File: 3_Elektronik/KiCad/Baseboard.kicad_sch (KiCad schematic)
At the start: 76 parts, among them J1 Conn_02x10_Odd_Even, J2 Conn_02x10_Odd_Even, J3 Conn_02x10_Odd_Even, J4 Conn_02x10_Odd_Even, J5 PinHeader 2,54mm 3p, J6 693072010801, J7 629722000214, Q1 2N7002K, Q2 2N7002K, SW2 430481025816, SW3 430481025816, U1 LSM6DSV320XTR, U2 TPS7B8601QDDARQ1, U3 TCAN334, U4 ESP32-S3-WROOM-1, U5 LSM6DSO32XTR, U6 DPS310, U7 IST8310, U8 CH224A

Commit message: fix: :bug: use LIS3MDL mag
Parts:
- C21: value 4.7µF -> 1µF
- U7: value IST8310 -> LIS3MDL; footprint Package_LGA:LGA-16_3x3mm_P0.5mm -> Package_LGA:LGA-12_2x2mm_P0.5mm; symbol Sensor_Magnetic:IST8310 -> Sensor_Magnetic:LIS3MDL
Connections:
- net +3V3: now also C21.1, C24.1, U7.10 (~{CS}), U7.5 (Vdd), U7.6 (Vdd_IO); no longer C20.1, C24.2, U7.13 (DVDD), U7.2 (AVDD)
- net BARO_INT: now also U4.24 (IO47); no longer U4.25 (IO48)
- net GND: now also C20.1, C24.2, U7.12 (GND), U7.2 (GND), U7.3 (GND); no longer C20.2, C24.1, U7.11 (VSS)
- net I2C0_SDA: now also U7.11 (SDA/SDI/SDO); no longer U7.16 (SDA)
- net IMU_INT: now also U4.23 (IO21); no longer U4.24 (IO47)
- net at U7.4 (C1): now also C20.2
- net MAG_DRDY: now reaches U7.8 (DRDY)
- net MAG_DRDY: now also U4.25 (IO48)
- no-connect marks 19 -> 14
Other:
- note added: "0x1C"
- note added: "STM LIS3MDL"
- note removed: "0x0E"
- note removed: "isentek IST8310"
- moved on the sheet: C20, C21, C24

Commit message: ci(drc): :green_heart: fix errors
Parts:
- J7: symbol Connector_Wurth_WR-USB:629722000214 -> AUXSPACE:629722000214
- U1: footprint LGA-14L_2p5X3X0p83_STM -> AUXSPACE:LGA-14L_2p5X3X0p83_STM; symbol 2026-10-07_23-10-11:LSM6DSV320XTR -> AUXSPACE:LSM6DSV320XTR
- U3: symbol Interface_CAN_LIN:TCAN334 -> AUXSPACE:TCAN334
- U4: footprint RF_Module:ESP32-S3-WROOM-1 -> AUXSPACE:ESP32-S3-WROOM-1; symbol RF_Module:ESP32-S3-WROOM-1 -> AUXSPACE:ESP32-S3-WROOM-1
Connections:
- net ACCEL_INT2: no longer names the net of U1.9 (INT2)
- no-connect marks 14 -> 15

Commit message: feat: :sparkles: new switches
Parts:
- J5: value PinHeader 2,54mm 3p -> Conn_01x04_Pin; footprint Connector_PinHeader_2.54mm:PinHeader_1x03_P2.54mm_Vertical -> (none); symbol Connector:Conn_01x03_Pin -> Connector:Conn_01x04_Pin; Part Number 61300311121 -> (none); USEAGE UART -> (none); WE_PTNBR 61300311121 -> (none)
- SW2, SW3: value 430481025816 -> 434331013822; footprint AUXSPACE:SW_Wurth_WS-TASV_430481025816 -> AUXSPACE:SW_Wurth_WS-TASU_434331013822; symbol AUXSPACE:430481025816 -> AUXSPACE:434331013822; Actuator Color Black -> White; Created Date 20260204 -> 20260310; Electrical Life (Cycles) 1000000 -> (none); Electrical Life(Cycles) (none) -> 100000 Cycles; H (mm) 2.5 -> (none); H(mm) (none) -> 1.35 mm; Operation Force (g) 160.0 -> (none); Operation Force(g) (none) -> 220 g; Part Number 430481025816 -> 434331013822; Series WS-TASV -> WS-TASU; USEAGE RESET -> (none); Vaporphase process not specified -> (none); WE_PTNBR 430481025816 -> (none); Washable Yes -> No
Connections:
- net GND: now also SW2.1, SW2.2; no longer SW2.3, SW2.4
- net Power Fault: now also U4.32 (IO39); no longer U4.31 (IO38)
- net RX: now also J5.4 (Pin_4); no longer J5.3 (Pin_3)
- net SD_CMD_MOSI: now also U4.33 (IO40); no longer U4.32 (IO39)
- net STATE_LED: now also U4.31 (IO38); no longer U4.33 (IO40)
- net TX: now also J5.3 (Pin_3); no longer J5.2 (Pin_2)
- net VBus_direct: now also J5.2 (Pin_2)
- net at R23.2, SW3.3, SW3.4: now also SW3.5, SW3.6
- net at C13.1, R15.2, U4.3 (EN): now also SW2.3, SW2.4, SW2.5, SW2.6; no longer SW2.1, SW2.2
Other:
- moved on the sheet: C13, R15, R23, SW2, SW3

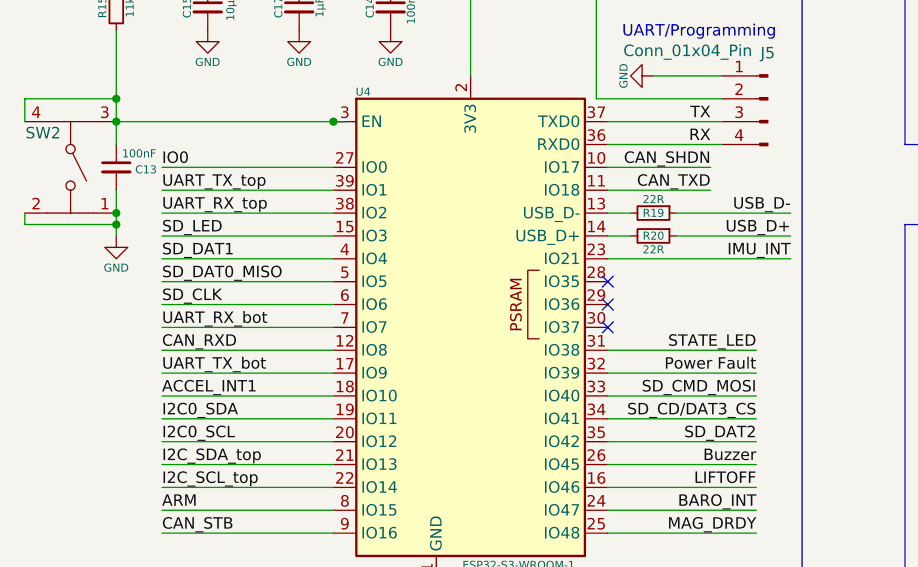
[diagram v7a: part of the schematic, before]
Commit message: feat: :sparkles: add auxolotl
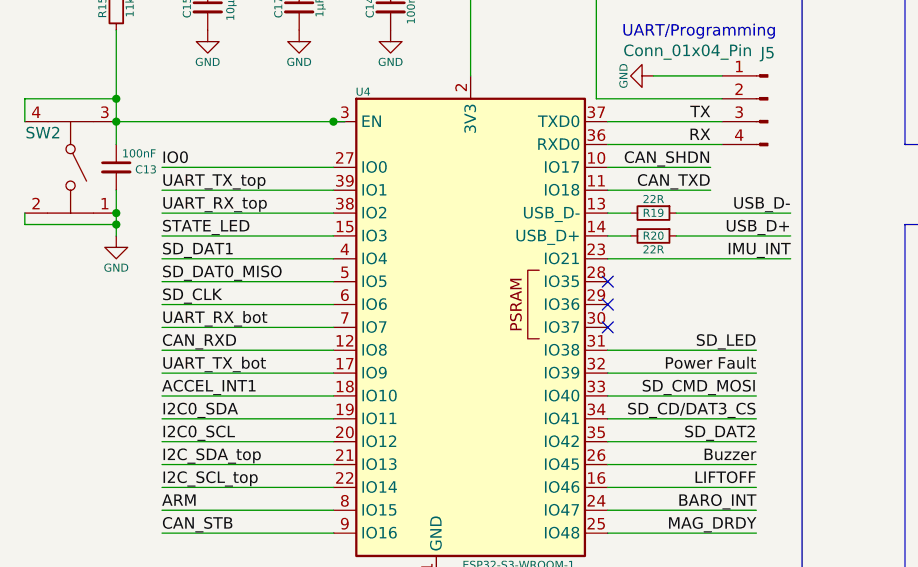
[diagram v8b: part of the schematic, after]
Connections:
- net SD_LED: now also U4.31 (IO38); no longer U4.15 (IO3)
- net STATE_LED: now also U4.15 (IO3); no longer U4.31 (IO38)
